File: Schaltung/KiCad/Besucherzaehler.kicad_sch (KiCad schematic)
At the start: 5 parts, among them J1 Pfosten OLED, J2 Pfosten DC-Wandler, J3 Pfosten Lichtschranke, J4 Pfosten, U1 WeMos_D1_mini

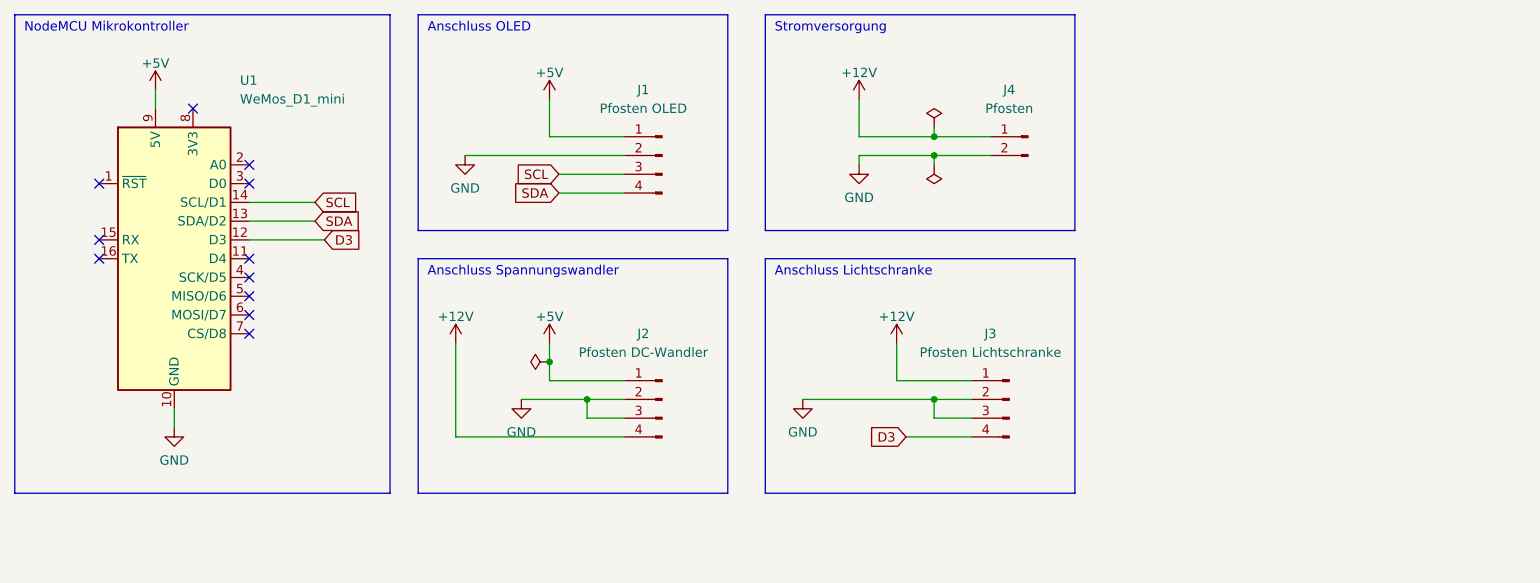
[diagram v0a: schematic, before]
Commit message: Schaltplan um Spannungsmessung erweitert
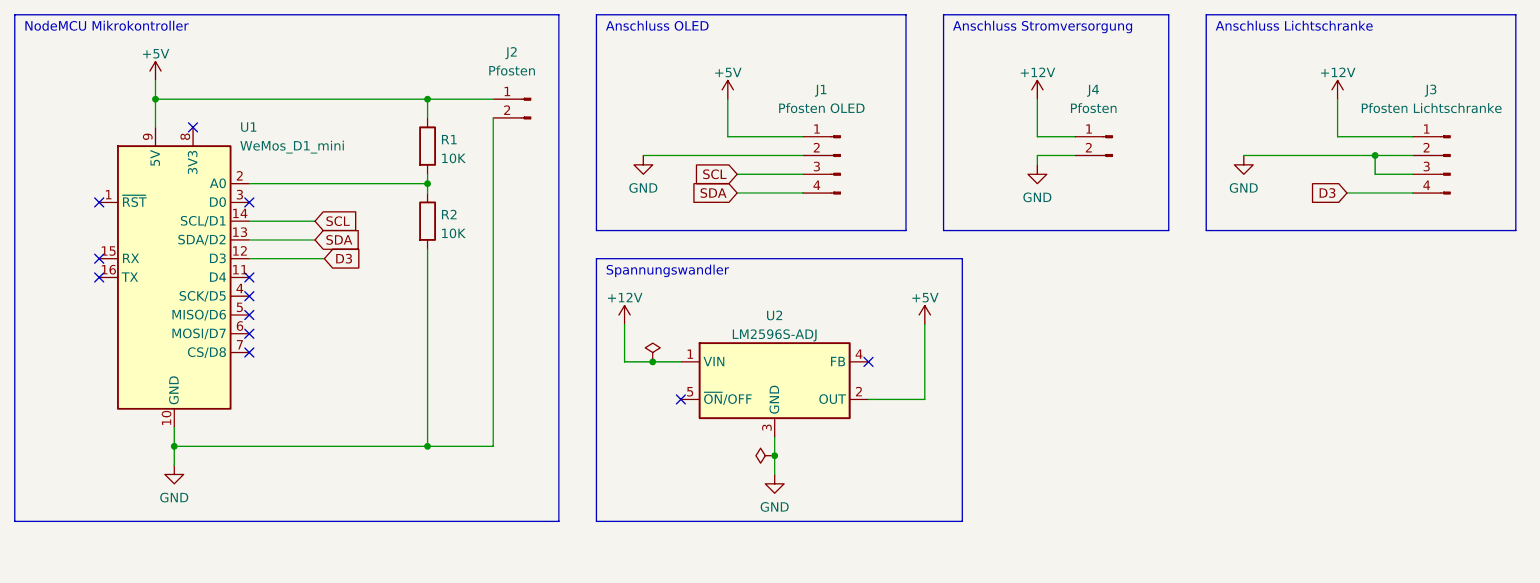
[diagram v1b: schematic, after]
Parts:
- removed J2: Pfosten DC-Wandler, symbol Connector:Conn_01x04_Male
- added J2: Pfosten, symbol Connector:Conn_01x02_Male
- added R1, R2: 10K, symbol Device:R
- added U2: LM2596S-ADJ, Package_TO_SOT_SMD:TO-263-5_TabPin3, symbol Regulator_Switching:LM2596S-ADJ
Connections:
- net +12V: now also U2.1 (VIN)
- net +5V: now also J2.1 (Pin_1), R1.1, U2.2 (OUT)
- net GND: now also J2.2 (Pin_2), R2.2, U2.3 (GND)
- net at U1.2 (A0): now also R1.2, R2.1
- no-connect marks 11 -> 12
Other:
- note added: "Anschluss Stromversorgung"
- note added: "Spannungswandler"
- note removed: "Anschluss Spannungswandler"
- note removed: "Stromversorgung"
- moved on the sheet: J1, J3, J4, U1

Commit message: Eingang der Lichtschranke auf D5 geändert
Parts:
- added R3: 10K, symbol Device:R
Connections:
- net D5: now reaches U1.4 (SCK/D5)
- net D5: now also J3.4 (Pin_4), R3.1
- net +3V3: now reaches U1.8 (3V3)
- net +3V3: now also R3.2
- net D3: no longer names the net of U1.12 (D3)
- net D3: no longer J3.4 (Pin_4)
- no-connect marks 12 -> 11
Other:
- moved on the sheet: R1, R2, U1
